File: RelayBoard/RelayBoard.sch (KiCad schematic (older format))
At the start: 64 parts, among them J1 Micro_SD_Card, J10 Conn_01x04_Male, J11 Conn_01x04_Male, J13 Conn_01x04_Male, J2 Screw_Terminal_01x02, J3 Conn_01x04_Male, J4 Conn_01x04_Male, J5 Conn_01x04_Male, J7 SI-52008-F, J8 SI-52008-F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

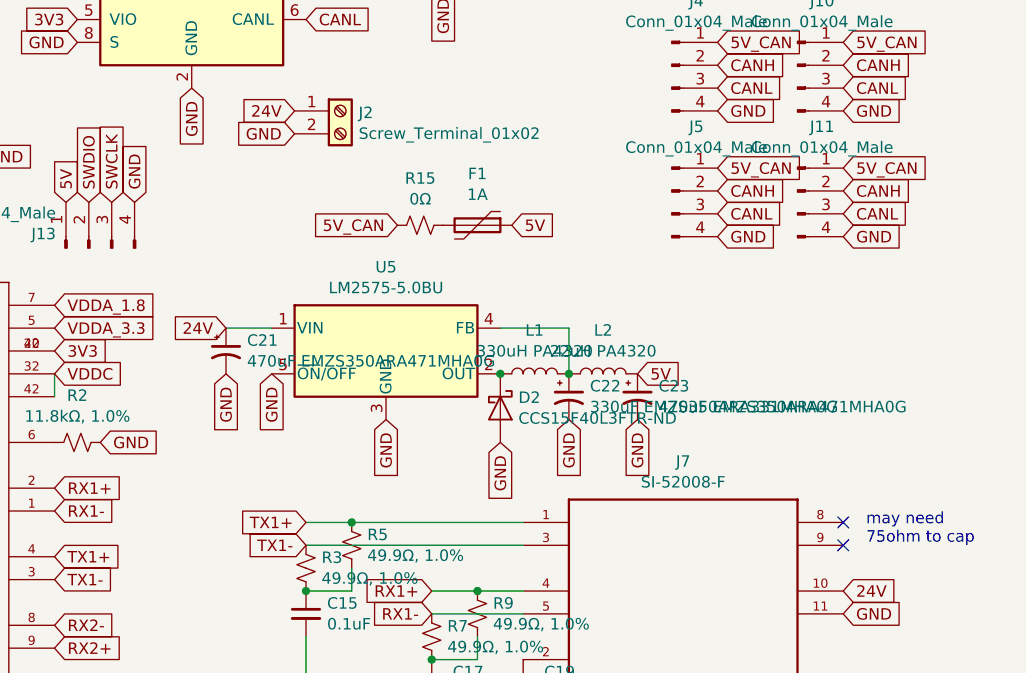
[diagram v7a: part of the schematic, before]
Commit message: ok give up on trying to regulate 24 to 5
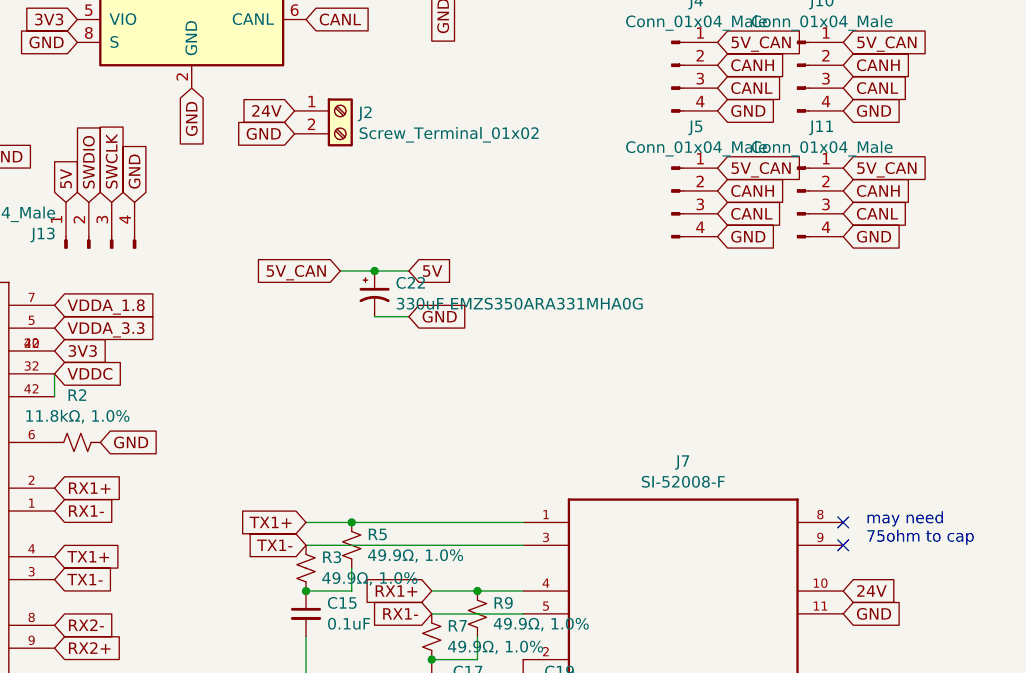
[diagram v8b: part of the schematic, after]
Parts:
- removed C21, C23: 470uF EMZS350ARA471MHA0G, Capacitor_SMD:CP_Elec_10x10, symbol Device:CP1_Small
- removed D2: CCS15F40L3FTR-ND, Diode_SMD:D_0603_1608Metric_Pad1.05x0.95mm_HandSolder, symbol Device:D_Schottky
- removed F1: 1A, Fuse:Fuse_0805_2012Metric_Pad1.15x1.40mm_HandSolder, symbol Device:Polyfuse
- removed L1: 330uH PA4320, Inductor_SMD:L_Pulse_PA4320, symbol Device:L
- removed L2: 22uH PA4320, Inductor_SMD:L_Pulse_PA4320, symbol Device:L
- removed R15: 0Ω, Jumper:SolderJumper-2_P1.3mm_Open_TrianglePad1.0x1.5mm, symbol Device:R_Small_US
- removed U5: LM2575-5.0BU, Package_TO_SOT_SMD:TO-263-5_TabPin3, symbol Regulator_Switching:LM2575-5.0BU
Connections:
- net 5V_CAN is gone; now on net +5V: J10.1 (Pin_1), J11.1 (Pin_1), J3.1 (Pin_1), J4.1 (Pin_1), J5.1 (Pin_1), J9.1 (Pin_1)
- net +5V: now also C22.1
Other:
- moved on the sheet: C22
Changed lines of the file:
@@
 Text GLabel 6350 3900 2    50   Input ~ 0
 RX2-
-$Comp
-L Device:CP1_Small C21
-U 1 1 5E84FFB9
-P 7100 2700
-F 0 "C21" H 7192 2746 50  0000 L CNN
-F 1 "470uF EMZS350ARA471MHA0G" H 7192 2655 50  0000 L CNN
-F 2 "Capacitor_SMD:CP_Elec_10x10" H 7100 2700 50  0001 C CNN
-F 3 "~" H 7100 2700 50  0001 C CNN
-	1    7100 2700
-	1    0    0    -1
-$EndComp
-Text GLabel 7800 3000 3    50   Input ~ 0
-GND
-$Comp
-L Regulator_Switching:LM2575-5.0BU U5
-U 1 1 5E84DD3F
-P 7800 2700
-F 0 "U5" H 7800 3067 50  0000 C CNN
-F 1 "LM2575-5.0BU" H 7800 2976 50  0000 C CNN
-F 2 "Package_TO_SOT_SMD:TO-263-5_TabPin3" H 7800 2450 50  0001 L CIN
-F 3 "http://ww1.microchip.com/downloads/en/DeviceDoc/lm2575.pdf" H 7800 2700 50  0001 C CNN
-	1    7800 2700
-	1    0    0    -1
-$EndComp
-Text GLabel 7300 2800 3    50   Input ~ 0
-GND
-Wire Wire Line
-	7100 2600 7300 2600
-Text GLabel 7100 2600 0    50   Input ~ 0
-24V
-Text GLabel 7100 2800 3    50   Input ~ 0
-GND
-$Comp
-L Device:L L1
-U 1 1 5E8687D9
-P 8450 2800
-F 0 "L1" V 8640 2800 50  0000 C CNN
-F 1 "330uH PA4320" V 8549 2800 50  0000 C CNN
-F 2 "Inductor_SMD:L_Pulse_PA4320" H 8450 2800 50  0001 C CNN
-F 3 "~" H 8450 2800 50  0001 C CNN
-	1    8450 2800
-	0    -1   -1   0
-$EndComp
-$Comp
-L Device:CP1_Small C22
-U 1 1 5E86EE8D
-P 8600 2900
-F 0 "C22" H 8692 2946 50  0000 L CNN
-F 1 "330uF EMZS350ARA331MHA0G" H 8692 2855 50  0000 L CNN
-F 2 "Capacitor_SMD:CP_Elec_10x10" H 8600 2900 50  0001 C CNN
-F 3 "~" H 8600 2900 50  0001 C CNN
-	1    8600 2900
-	1    0    0    -1
-$EndComp
-Wire Wire Line
-	8300 2600 8600 2600
-Wire Wire Line
-	8600 2600 8600 2800
-Connection ~ 8600 2800
-Text GLabel 8300 3100 3    50   Input ~ 0
-GND
-Text GLabel 8600 3000 3    50   Input ~ 0
-GND
-Text GLabel 7850 2150 0    50   Input ~ 0
-5V_CAN
 Text GLabel 1650 6900 0    50   Input ~ 0
 24V
@@
 Text GLabel 6700 2050 1    50   Input ~ 0
 GND
-$Comp
-L Device:R_Small_US R15
-U 1 1 5E863A07
-P 7950 2150
-F 0 "R15" V 7745 2150 50  0000 C CNN
-F 1 "0Ω" V 7836 2150 50  0000 C CNN
-F 2 "Jumper:SolderJumper-2_P1.3mm_Open_TrianglePad1.0x1.5mm" H 7950 2150 50  0001 C CNN
-F 3 "~" H 7950 2150 50  0001 C CNN
-	1    7950 2150
-	0    1    1    0
-$EndComp
 Text GLabel 3150 1250 2    50   Input ~ 0
 MDIO
@@
 	3950 5100 4350 5100
 NoConn ~ 4350 5500
-Text GLabel 8350 2150 2    50   Input ~ 0
+$Comp
+L Device:CP1_Small C22
+U 1 1 5E86EE8D
+P 7750 2450
+F 0 "C22" H 7842 2496 50  0000 L CNN
+F 1 "330uF EMZS350ARA331MHA0G" H 7842 2405 50  0000 L CNN
+F 2 "Capacitor_SMD:CP_Elec_10x10" H 7750 2450 50  0001 C CNN
+F 3 "~" H 7750 2450 50  0001 C CNN
+	1    7750 2450
+	1    0    0    -1
+$EndComp
+Text GLabel 7600 2350 0    50   Input ~ 0
+5V_CAN
+Text GLabel 7900 2550 2    50   Input ~ 0
+GND
+Text GLabel 7900 2350 2    50   Input ~ 0
 5V
-$Comp
-L Device:Polyfuse F1
-U 1 1 5EA76ED7
-P 8200 2150
-F 0 "F1" V 7975 2150 50  0000 C CNN
-F 1 "1A" V 8066 2150 50  0000 C CNN
-F 2 "Fuse:Fuse_0805_2012Metric_Pad1.15x1.40mm_HandSolder" H 8250 1950 50  0001 L CNN
-F 3 "~" H 8200 2150 50  0001 C CNN
-	1    8200 2150
-	0    1    1    0
-$EndComp
-Text GLabel 8900 2800 2    50   Input ~ 0
-5V
-$Comp
-L Device:L L2
-U 1 1 5EA957DB
-P 8750 2800
-F 0 "L2" V 8940 2800 50  0000 C CNN
-F 1 "22uH PA4320" V 8849 2800 50  0000 C CNN
-F 2 "Inductor_SMD:L_Pulse_PA4320" H 8750 2800 50  0001 C CNN
-F 3 "~" H 8750 2800 50  0001 C CNN
-	1    8750 2800
-	0    -1   -1   0
-$EndComp
-Text GLabel 8900 3000 3    50   Input ~ 0
-GND
-$Comp
-L Device:D_Schottky D2
-U 1 1 5EA9FF6A
-P 8300 2950
-F 0 "D2" V 8254 3029 50  0000 L CNN
-F 1 "CCS15F40L3FTR-ND" V 8345 3029 50  0000 L CNN
-F 2 "Diode_SMD:D_0603_1608Metric_Pad1.05x0.95mm_HandSolder" H 8300 2950 50  0001 C CNN
-F 3 "~" H 8300 2950 50  0001 C CNN
-	1    8300 2950
-	0    1    1    0
-$EndComp
-Connection ~ 8300 2800
-$Comp
-L Device:CP1_Small C23
-U 1 1 5EA957E1
-P 8900 2900
-F 0 "C23" H 8992 2946 50  0000 L CNN
-F 1 "470uF EMZS350ARA471MHA0G" H 8992 2855 50  0000 L CNN
-F 2 "Capacitor_SMD:CP_Elec_10x10" H 8900 2900 50  0001 C CNN
-F 3 "~" H 8900 2900 50  0001 C CNN
-	1    8900 2900
-	1    0    0    -1
-$EndComp
+Wire Wire Line
+	7600 2350 7750 2350
+Connection ~ 7750 2350
+Wire Wire Line
+	7750 2350 7900 2350
+Wire Wire Line
+	7750 2550 7900 2550
 $EndSCHEMATC
